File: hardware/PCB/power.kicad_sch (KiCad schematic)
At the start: 63 parts, among them J1 24V LED Strip, J2 24V FAN XYJ24B4010M, J3 Power Entry, U1 TPS62933, U2 XL4015 Regulator Module, U3 XL4015 Regulator Module, U4 TPS56837Hx, U5 XL4015 Regulator Module, U6 TPS56837Hx

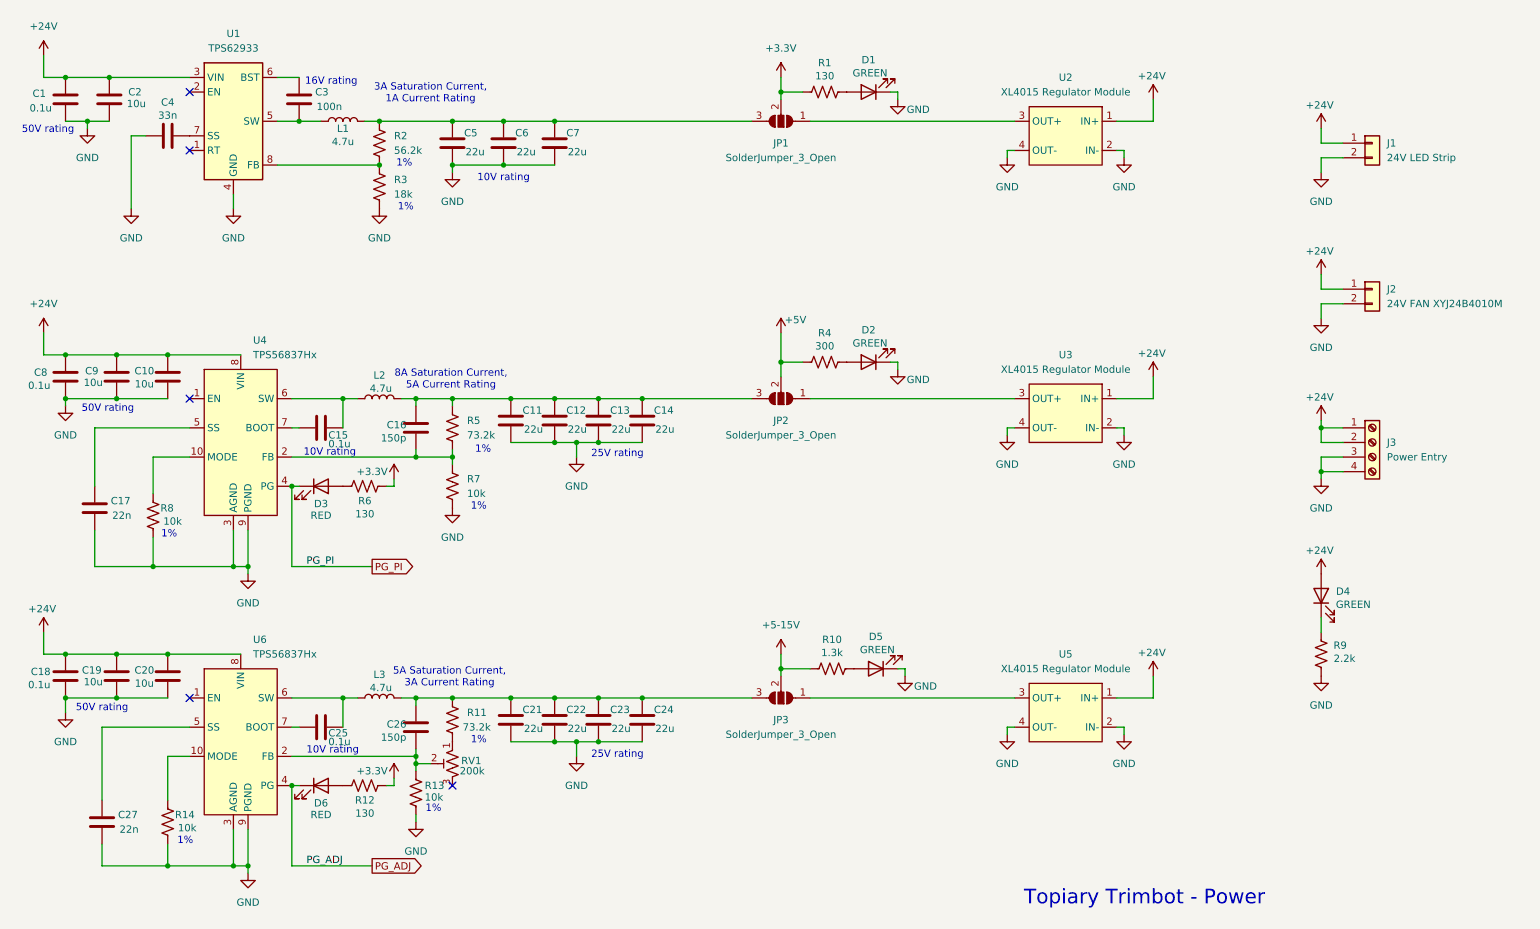
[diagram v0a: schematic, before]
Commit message: Finish first pass placement of parts on PCB, several updates and fixes to schematic included
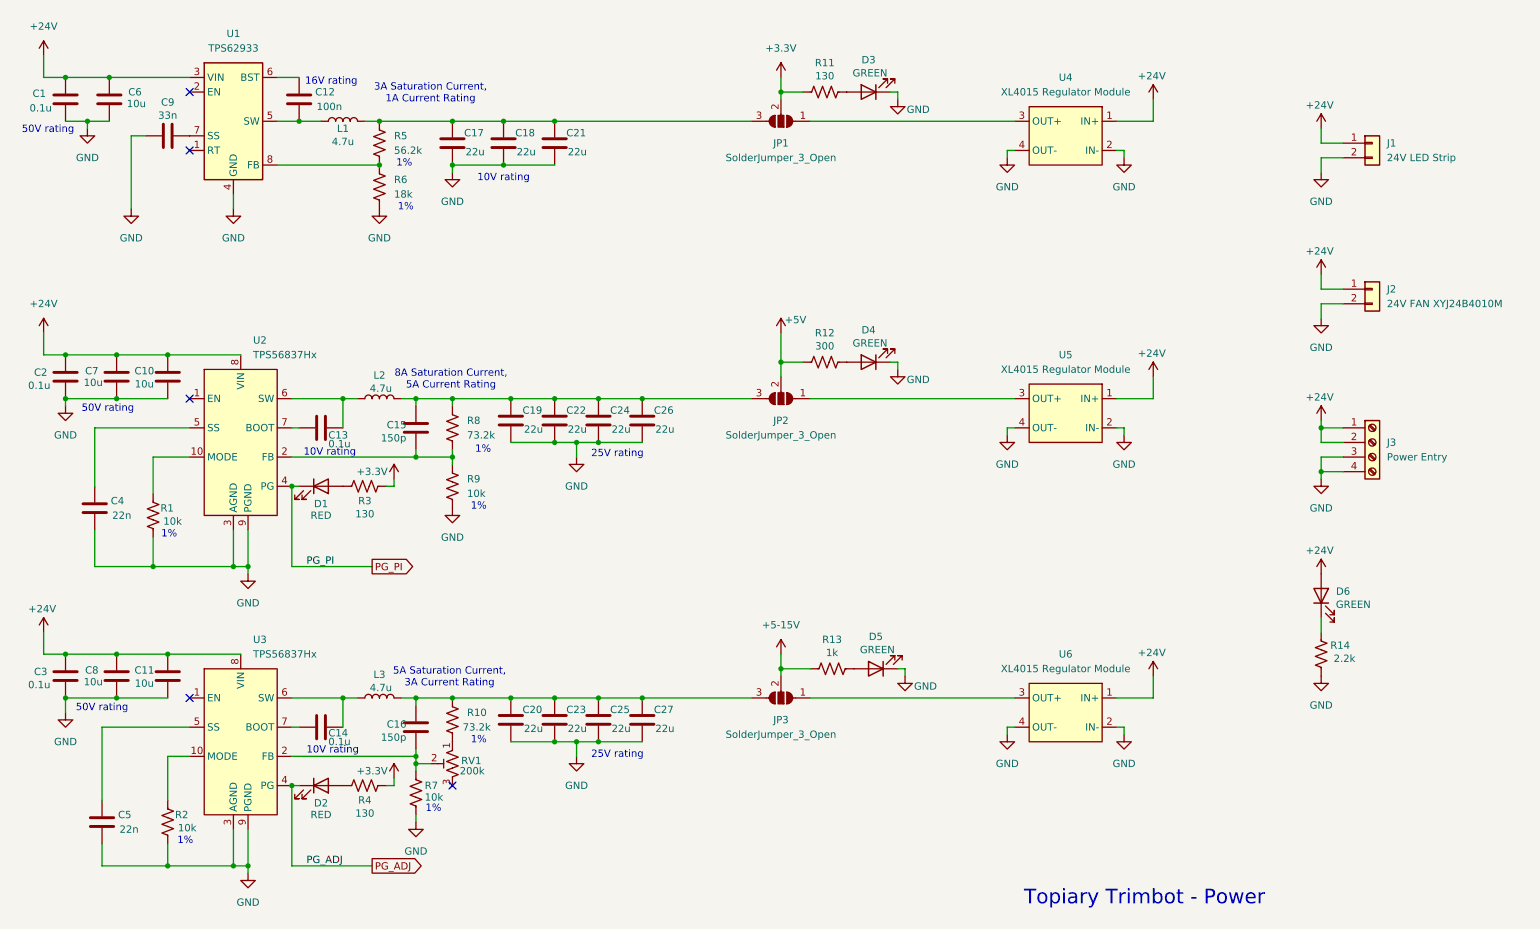
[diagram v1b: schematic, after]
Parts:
- JP1, JP2, JP3: footprint Jumper:SolderJumper-3_P2.0mm_Open_TrianglePad1.0x1.5mm -> CustomFootprints:SolderJumper-3_P1.5mm_Open_RoundedPad1.0x1.5mm
- R13: renamed from R10; value 1.3k -> 1k
- renumbered C20 to C11, C3 to C12, C15 to C13, C25 to C14, C16 to C15, C26 to C16, C5 to C17, C6 to C18, C11 to C19, C8 to C2, C21 to C20, C7 to C21, C12 to C22, C22 to C23, C13 to C24, C23 to C25, C14 to C26, C24 to C27, C18 to C3, C17 to C4, C27 to C5, C2 to C6, C9 to C7, C19 to C8, C4 to C9, D3 to D1, D6 to D2, D1 to D3, D2 to D4, D4 to D6, R8 to R1, R11 to R10, R1 to R11, R4 to R12, R9 to R14, R14 to R2, R6 to R3, R12 to R4, R2 to R5, R3 to R6, R13 to R7, R5 to R8, R7 to R9, U4 to U2, U6 to U3, U2 to U4, U3 to U5, U5 to U6

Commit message: Continue layout, including swapping to linear BL driver
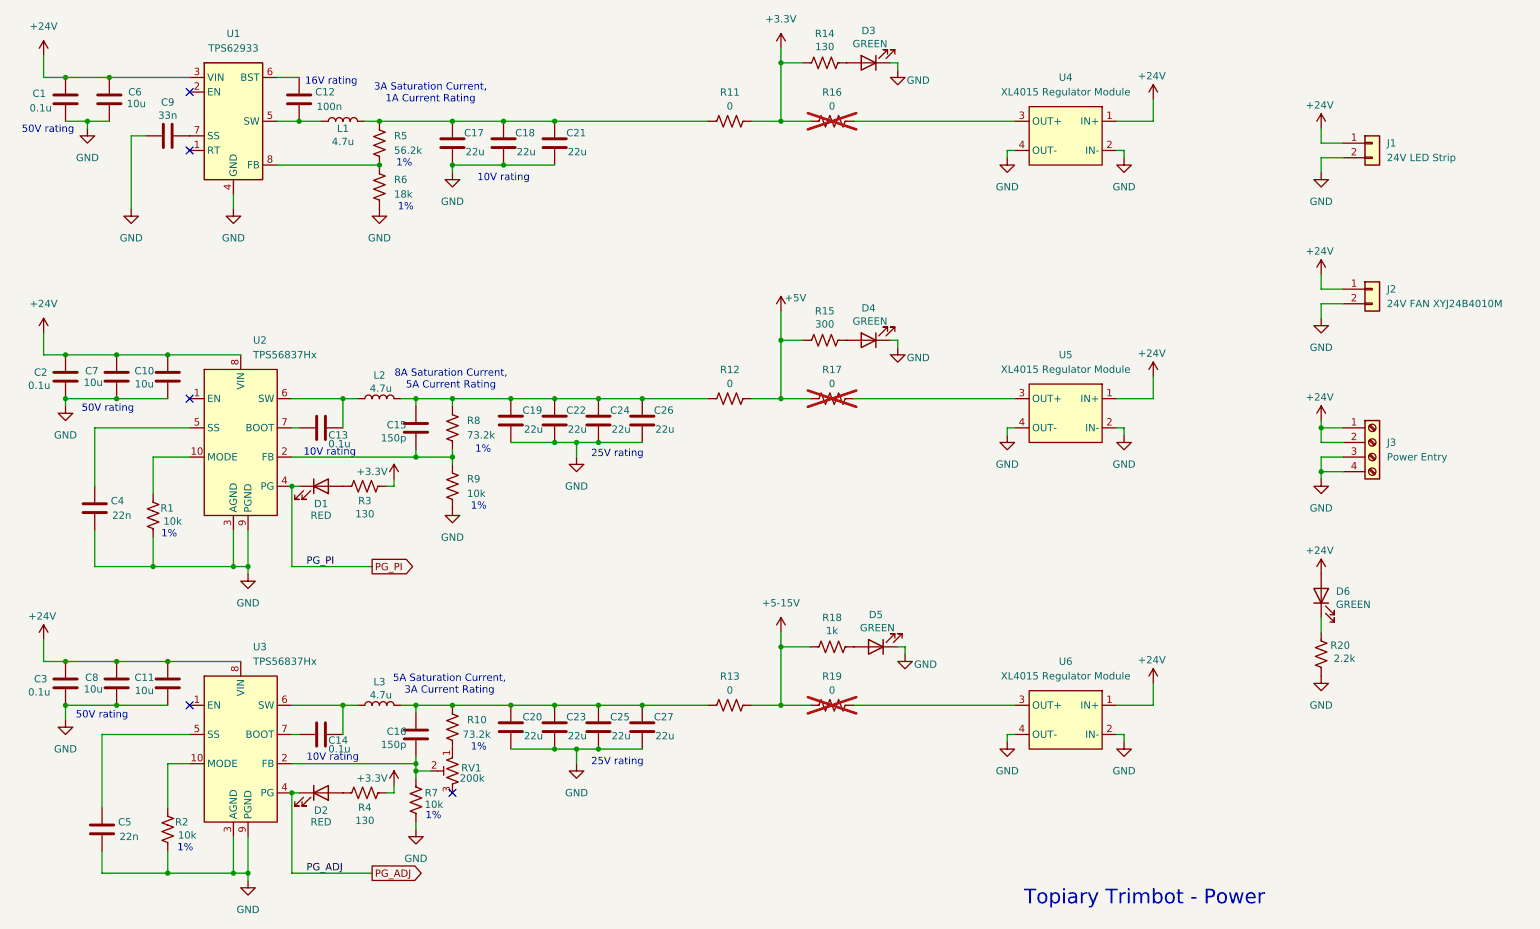
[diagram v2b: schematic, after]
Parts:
- removed JP1, JP2, JP3: SolderJumper_3_Open, CustomFootprints:SolderJumper-3_P1.5mm_Open_RoundedPad1.0x1.5mm, symbol Jumper:SolderJumper_3_Open
- added R11, R12, R13, R16, R17, R19: 0, Resistor_SMD:R_2010_5025Metric, symbol Device:R_US
- renumbered R11 to R14, R12 to R15, R13 to R18, R14 to R20
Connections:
- net +3.3V: now also R11.2, R16.1
- net +5-15V: now also R13.2, R19.1
- net +5V: now also R12.2, R17.1
- net at U4.3 (OUT+): now also R16.2
- net at U6.3 (OUT+): now also R19.2
- net at C16.1, C20.1, C23.1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: now also R13.1
- net at C15.1, C19.1, C22.1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: now also R12.1
- net at U5.3 (OUT+): now also R17.2
- net at C17.1, C18.1, C21.1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: now also R11.1
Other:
- moved on the sheet: C11, C14, C16, C20, C23, C25, C27, C3, C5, C8, D2, D3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

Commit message: all part numbers
may need revisions
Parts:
- C12: MANUFACTURER (none) -> Murata; Manufacturer_Part_Number (none) -> GCM21BR72A104KA37L
- C15, C16: MANUFACTURER (none) -> Murata; Manufacturer_Part_Number (none) -> GRM2165C1H151JA01D
- C4, C5: MANUFACTURER (none) -> Murata; Manufacturer_Part_Number (none) -> GRM21B5C1H223JA01L
- C9: MANUFACTURER (none) -> Murata; Manufacturer_Part_Number (none) -> GCM219R72A333KA37D
- D1, D2: MANUFACTURER (none) -> Wurth; Manufacturer_Part_Number (none) -> 150080RS75000
- D3, D4, D5, D6: value GREEN -> GRN; MANUFACTURER (none) -> Wurth; Manufacturer_Part_Number (none) -> 150080GS75000
- J1: MANUFACTURER (none) -> Molex; Manufacturer_Part_Number (none) -> 1718560102
- J2: MANUFACTURER (none) -> Wurth; Manufacturer_Part_Number (none) -> 61300211121
- J3: MANUFACTURER (none) -> TE Connectivity AMP Connectors; Manufacturer_Part_Number (none) -> 6DBL-04-006
- R1, R2, R7, R9: MANUFACTURER (none) -> Yageo; Manufacturer_Part_Number (none) -> RC0805JR-0710KL
- R10, R8: MANUFACTURER (none) -> Yageo; Manufacturer_Part_Number (none) -> RT0805BRD0773K2L
- R14, R3, R4: MANUFACTURER (none) -> Yageo; Manufacturer_Part_Number (none) -> RC0805JR-07130RL
- R15: MANUFACTURER (none) -> Yageo; Manufacturer_Part_Number (none) -> RC0805FR-07300RL
- R18: MANUFACTURER (none) -> Yageo; Manufacturer_Part_Number (none) -> RC0805FR-071KL
- R20: MANUFACTURER (none) -> Yageo; Manufacturer_Part_Number (none) -> RC0805FR-072K2L
- R5: MANUFACTURER (none) -> Yageo; Manufacturer_Part_Number (none) -> RT0805BRD0756K2L
- R6: MANUFACTURER (none) -> Yageo; Manufacturer_Part_Number (none) -> RT0805BRD0718KL
- U4, U5, U6: MANUFACTURER (none) -> Elecrow; Manufacturer_Part_Number (none) -> XL4015

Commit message: Final changes before submission to website
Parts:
- R8: value 73.2k -> 75k; Manufacturer_Part_Number RT0805BRD0773K2L -> RT0805DRD0775KL
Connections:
- net PG_PI renamed PG_5V
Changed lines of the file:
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@@
 	(text "1%"
 		(exclude_from_sim no)
-		(at 95.504 92.71 0)
+		(at 93.98 92.71 0)
 		(effects
 			(font
@@
 		)
 	)
-	(label "PG_PI"
+	(label "PG_5V"
 		(at 64.77 113.03 0)
 		(effects
@@
 		)
 	)
-	(global_label "PG_PI"
+	(global_label "PG_5V"
 		(shape output)
 		(at 76.2 113.03 0)
@@
 		)
 		(property "Intersheetrefs" "${INTERSHEET_REFS}"
-			(at 84.5676 113.03 0)
+			(at 84.9909 113.03 0)
 			(effects
 				(font
@@
 		(dnp no)
 		(property "Reference" "C14"
-			(at 68.58 143.256 90)
+			(at 72.39 140.716 90)
 			(effects
 				(font
@@
 		)
 		(property "Value" "0.1u"
-			(at 68.58 144.78 90)
+			(at 72.136 143.002 90)
 			(effects
 				(font
@@
 		(fields_autoplaced yes)
 		(property "Reference" "R8"
-			(at 92.71 87.6299 0)
+			(at 91.821 87.6878 0)
 			(effects
 				(font
@@
 			)
 		)
-		(property "Value" "73.2k"
-			(at 92.71 90.1699 0)
+		(property "Value" "75k"
+			(at 91.821 90.1121 0)
 			(effects
 				(font
@@
 			)
 		)
-		(property "Manufacturer_Part_Number" "RT0805BRD0773K2L"
+		(property "Manufacturer_Part_Number" "RT0805DRD0775KL"
 			(at 90.17 88.9 0)
 			(effects
@@
 		(dnp no)
 		(property "Reference" "C16"
-			(at 78.74 141.732 0)
+			(at 77.47 141.478 0)
 			(effects
 				(font
